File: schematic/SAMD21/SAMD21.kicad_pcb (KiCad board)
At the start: 4 copper layers, 100 x 100 mm, 54 parts, among them IC1 ATSAMD21G18A-AU, IC2 AZ1117IH-3.3TRG1, IC3 MCP2221-I_SL, J1 Barrel_Jack_Switch, J10 Conn_02x06_Odd_Even, J11 Conn_02x06_Odd_Even, J12 Conn_02x06_Odd_Even, J13 Conn_01x02, J14 Conn_02x05_Odd_Even, J15 Conn_01x08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

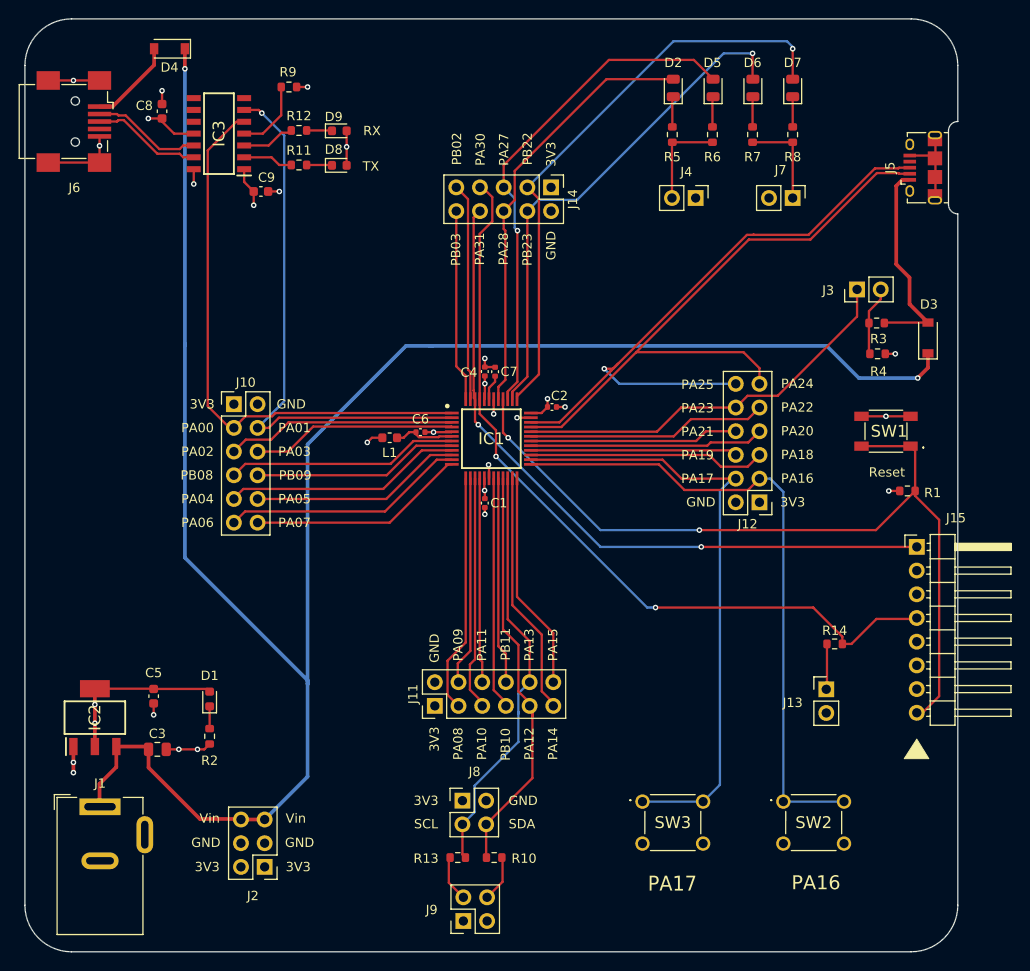
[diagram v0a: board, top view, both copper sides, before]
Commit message: Converted to KiCad 6
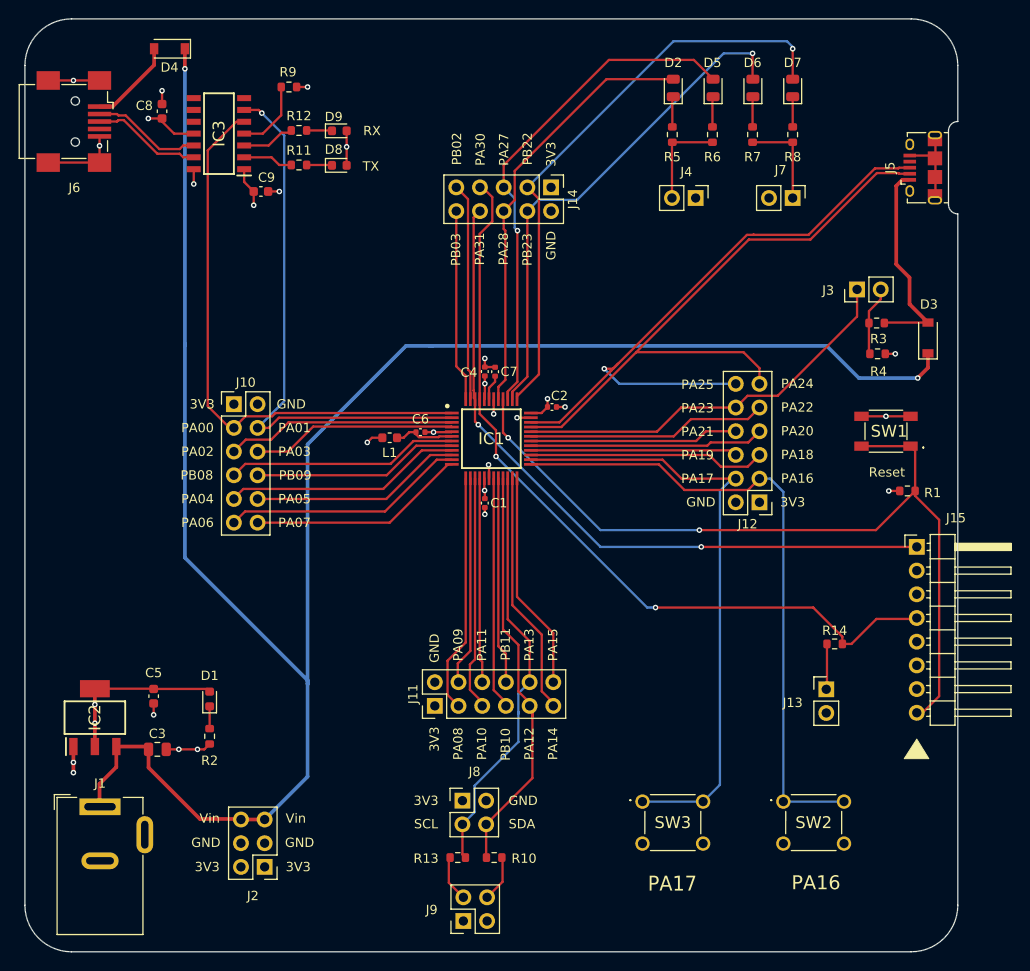
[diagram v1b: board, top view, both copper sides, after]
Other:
- net class Default removed
- net class Power removed
